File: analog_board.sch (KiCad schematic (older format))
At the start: 1 part

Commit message: Current measurement channels and connectors added
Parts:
- removed R?: R, symbol Device:R
- added C? (x2): 1n, symbol Device:C
- added C? (x6): 0.1u, symbol Device:C
- added C? (x6): 10u, symbol Device:C
- added D? (x2): LM385Z-1.2, Package_TO_SOT_THT:TO-92_Inline, symbol Reference_Voltage:LM385Z-1.2
- added J301, J302, J303, J304: SAMTEC-TSW-105-07-X-D, SAMTEC-TSW-105-07-X-D, symbol SAMTEC-TSW-105-07-X-D:SAMTEC-TSW-105-07-X-D
- added J? (x2): Conn_01x03_Male, symbol Connector:Conn_01x03_Male
- added R? (x2): 10M, symbol Device:R
- added R? (x6): 10R, symbol Device:R
- added R? (x2): 470R, symbol Device:R
- added R? (x4): 1k, symbol Device:R
- added R? (x2): 1k5, symbol Device:R
- added U? (x2): AD620, symbol Amplifier_Instrumentation:AD620
- added U? (x5): LM324, symbol Amplifier_Operational:LM324
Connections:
- net +15V: now also C?.1, C?.1, C?.1, C?.1, C?.1, C?.1, J301.7, J?.1 (Pin_1), J?.1 (Pin_1), U?.4 (V+), U?.7 (Vs+), U?.7 (Vs+)
- net GND: now also C?.1, C?.1, C?.2, C?.2, C?.2, C?.2, C?.2, C?.2, C?.2, C?.2, C?.2, C?.2, C?.2, C?.2, D?.2 (K), D?.2 (K), R?.1, R?.1, R?.1, R?.1, R?.1, R?.1, R?.2, R?.2, U?.2 (-), U?.2 (-), U?.2 (-), U?.2 (-)
- new net: R?.1, U?.1 (Rg) (x2)
- new net: C?.2, R?.1, U?.3 (+) (x2)
- new net: U?.1, U?.5 (Ref) (x2)
- new net: U?.5 (+), U?.6 (x2)
- new net: R?.2, U?.8 (Rg) (x2)
- new net: D?.3 (A), R?.1 (x2)
- new net: R?.1, R?.2 (x2)
- new net: R?.1, R?.2, U?.3 (+) (x2)
- new net +5V: J301.1
- new net -15V: C?.1, C?.1, C?.1, C?.1, C?.1, C?.1, J301.9, J?.3 (Pin_3), J?.3 (Pin_3), U?.11 (V-), U?.4 (Vs-), U?.4 (Vs-)
- new net 3V3_REF: J301.5
- new net 5V_REF: J301.3
- new net Current_ch1_out: U?.6 (-), U?.7
- new net Current_ch2_out: U?.6 (-), U?.7
- new net Current_ch_1_out: J303.1
- new net Current_ch_2_out: J303.3
- new net Current_sensor_1: J302.1, J?.2 (Pin_2), R?.2, R?.2, R?.2, R?.2
- new net Current_sensor_2: J302.3, J?.2 (Pin_2), R?.2, R?.2, R?.2, R?.2
- new net DIG1: J304.1
- new net DIG2: J304.3
- new net DIG3: J304.5
- new net DIG4: J304.7
- new net DIG5: J304.9
- new net Torque_pedal_ADC: J303.5
- new net Torque_pedal_in: J302.5

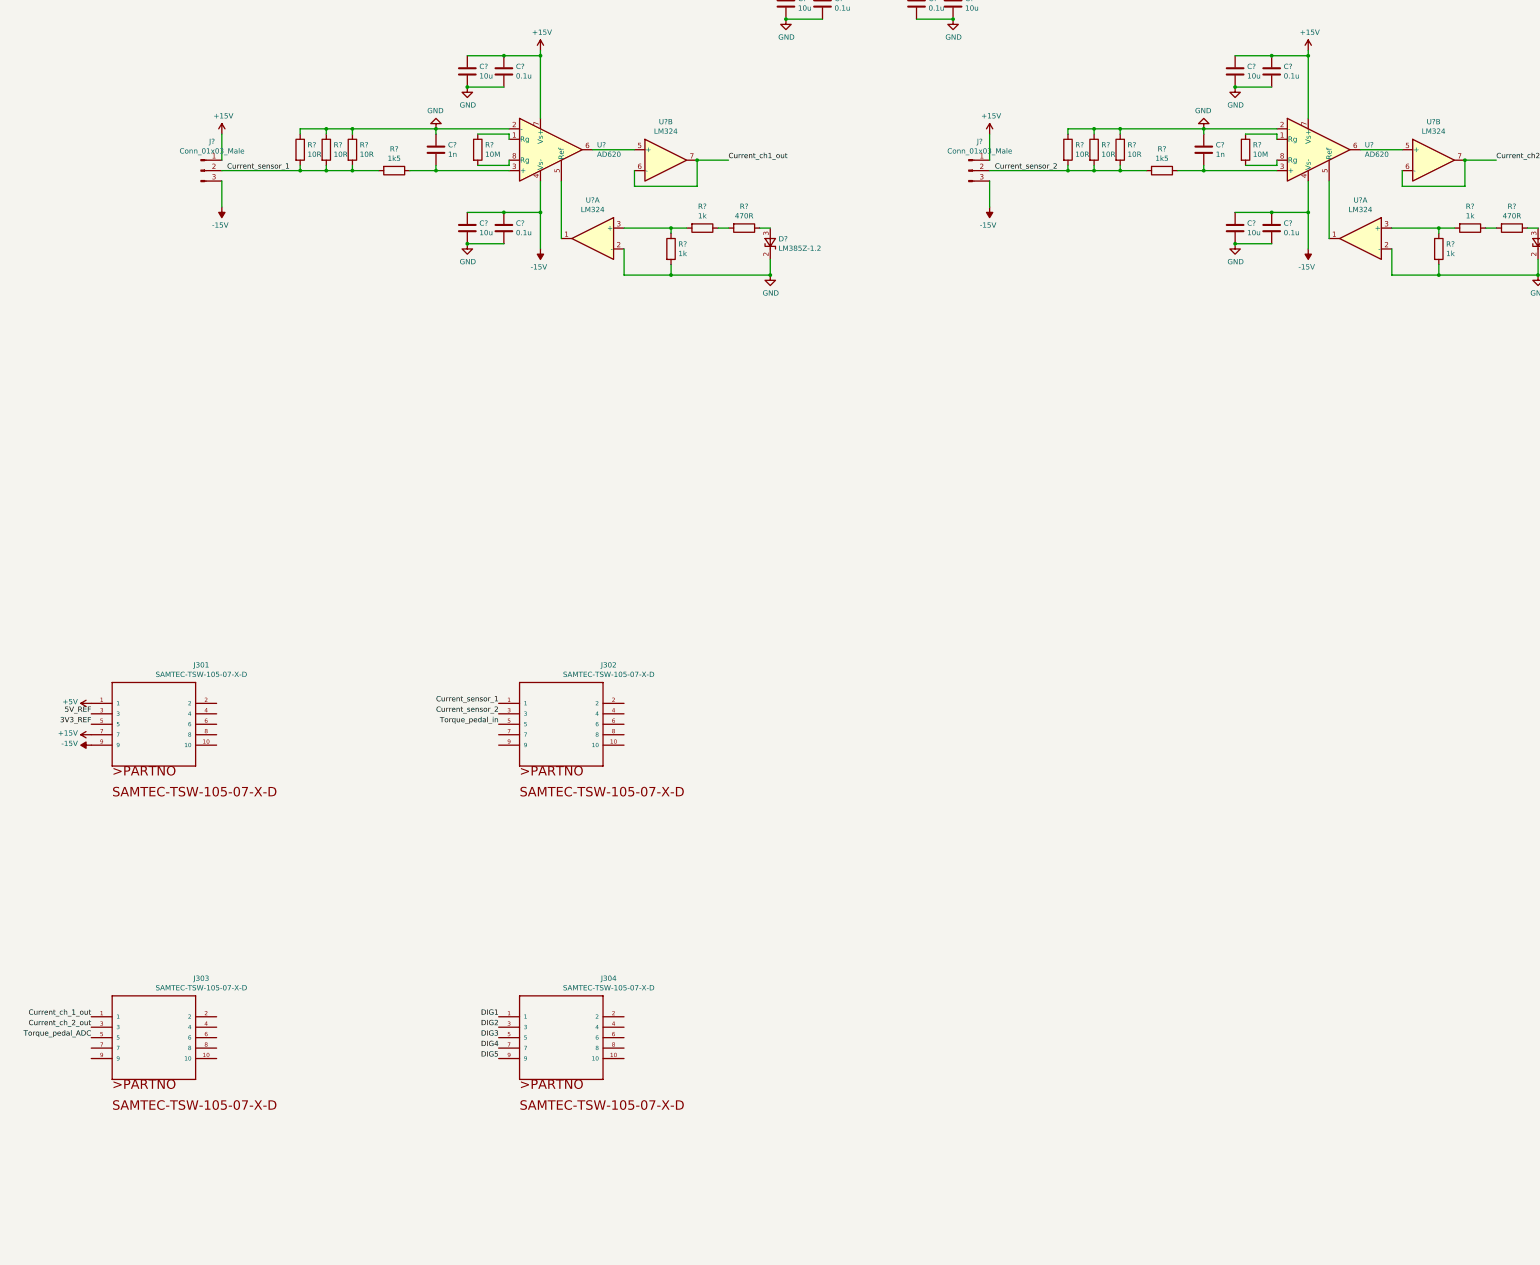
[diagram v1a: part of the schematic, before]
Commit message: Current measurement input filters, torque pedal reading
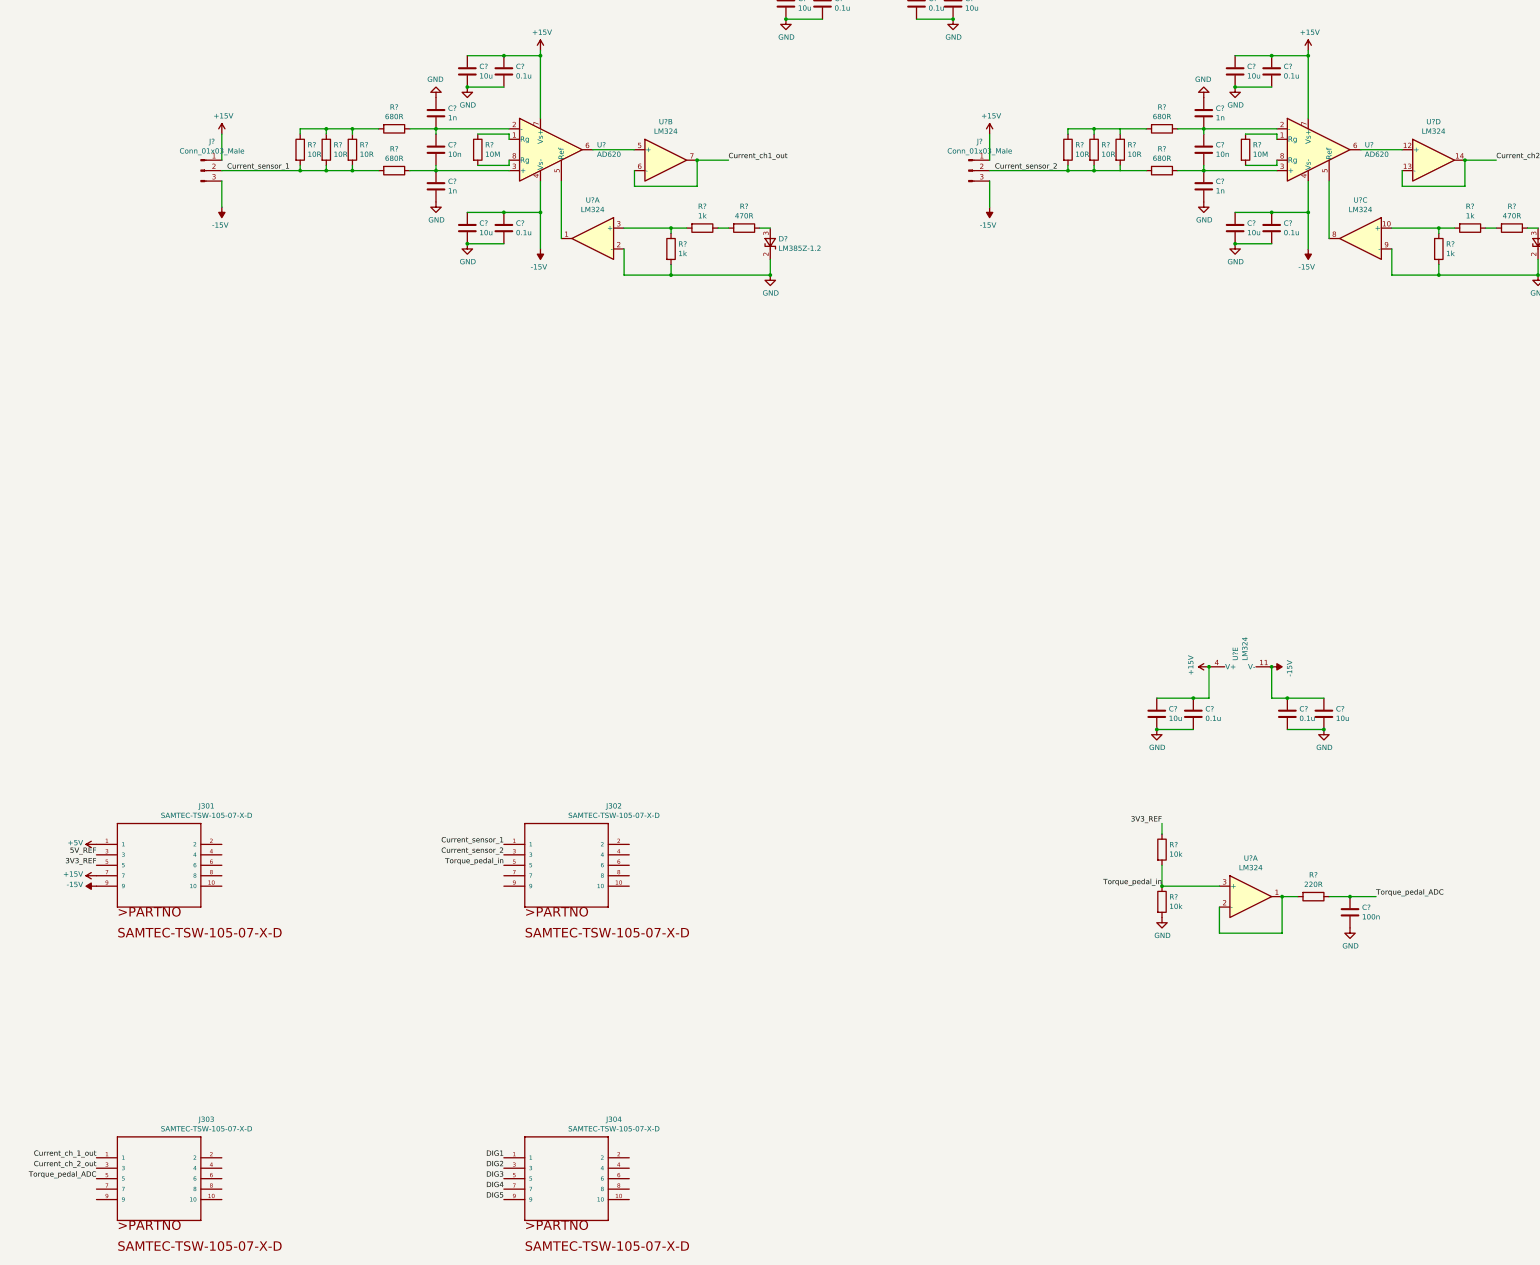
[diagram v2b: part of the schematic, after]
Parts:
- removed C?: 1n, symbol Device:C
- removed R?: 1k5, symbol Device:R
- removed U? (x2): LM324, symbol Amplifier_Operational:LM324
- added C? (x4): 1n, symbol Device:C
- added C?: 10n, symbol Device:C
- added C? (x2): 0.1u, symbol Device:C
- added C? (x2): 10u, symbol Device:C
- added C?: 100n, symbol Device:C
- added R? (x3): 680R, symbol Device:R
- added R?: 220R, symbol Device:R
- added R? (x2): 10k, symbol Device:R
- added U? (x4): LM324, symbol Amplifier_Operational:LM324
- C?: value 1n -> 10n
- R?: value 1k5 -> 680R
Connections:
- net +15V: now also C?.1, C?.1, U?.4 (V+)
- net -15V: now also C?.1, C?.1, U?.11 (V-)
- net 3V3_REF: now also R?.1
- net Current_ch2_out: now also U?.13 (-), U?.14
- net Current_sensor_2: now also R?.2
- net GND: now also C?.1, C?.1, C?.2, C?.2, C?.2, C?.2, C?.2, C?.2, C?.2, R?.2, U?.9 (-); no longer C?.1, R?.1, R?.1, R?.1, R?.1, R?.1, R?.1, U?.2 (-), U?.2 (-)
- net Torque_pedal_ADC: now also C?.1, R?.1
- net Torque_pedal_in: now also R?.1, R?.2, U?.3 (+)
- net at C?.2, R?.1, U?.3 (+): now also C?.1
- net at U?.3 (+): now also C?.1, C?.2, R?.1
- net at U?.5 (Ref): now also U?.8
- net at U?.6: now also U?.12 (+)
- net at R?.1, R?.2: now also U?.10 (+)
- new net: C?.1, C?.2, R?.1, U?.2 (-) (x2)
- new net: R?.1, R?.1, R?.1, R?.2 (x2)
- new net: R?.2, U?.1, U?.2 (-)
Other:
- moved on the sheet: J301, J302, J303, J304

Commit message: Added output filters and fixed reference opamp
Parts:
- removed C? (x2): 0.1u, symbol Device:C
- removed C? (x2): 10u, symbol Device:C
- removed D? (x2): LM385Z-1.2, Package_TO_SOT_THT:TO-92_Inline, symbol Reference_Voltage:LM385Z-1.2
- removed R? (x2): 10M, symbol Device:R
- removed R? (x2): 470R, symbol Device:R
- removed R? (x4): 1k, symbol Device:R
- removed U?: LM324, symbol Amplifier_Operational:LM324
- added C? (x4): 100n, symbol Device:C
- added C? (x2): 0.1u, symbol Device:C
- added C? (x2): 10u, symbol Device:C
- added D? (x2): LM385Z-1.2, Package_TO_SOT_THT:TO-92_Inline, symbol Reference_Voltage:LM385Z-1.2
- added R? (x2): 3k3, symbol Device:R
- added R? (x4): 220R, symbol Device:R
- added R? (x4): 1k, symbol Device:R
- added R? (x2): 470R, symbol Device:R
- added U? (x3): LM324, symbol Amplifier_Operational:LM324
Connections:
- net +15V: now also C?.1, C?.1, U?.4 (V+)
- net -15V: now also C?.1, C?.1, U?.11 (V-)
- net 3V3_REF: now also R?.1, R?.1
- net Current_ch1_out: now also C?.1, R?.1; no longer U?.6 (-), U?.7
- net Current_ch2_out: now also C?.1, R?.1; no longer U?.13 (-), U?.14
- net GND: now also R?.1, R?.1, R?.1, R?.1, R?.1, R?.1, R?.2, R?.2, C?.2, C?.2, C?.2, C?.2, C?.2, C?.2, C?.2, C?.2, D?.3 (A), D?.3 (A), R?.2, R?.2; no longer U?.2 (-), U?.9 (-)
- net at U?.1, U?.5 (Ref): now also U?.2 (-)
- net at U?.6: now also R?.2; no longer U?.5 (+)
- net at U?.3 (+): now also R?.1, R?.1
- net at U?.5 (Ref), U?.8: now also U?.9 (-)
- net at U?.6: now also R?.2; no longer U?.12 (+)
- net at U?.10 (+): now also R?.1, R?.1
- new net: C?.1, R?.1, U?.5 (+)
- new net: R?.2, U?.6 (-), U?.7
- new net: D?.2 (K), R?.2, U?.3 (+) (x2)
- new net: C?.1, R?.1, U?.12 (+)
- new net: R?.2, U?.13 (-), U?.14
- new net: R?.2, U?.1, U?.2 (-) (x2)
- new net: R?.1, R?.2 (x2)
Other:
- moved on the sheet: C?, J?, R?, U?, U?A, U?B, U?C, U?D, U?E

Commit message: Fixed opamp parts to the corresponding package
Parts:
- gave numbers to parts that had none: 2
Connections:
- net Torque_pedal_in: now also U1.12 (+); no longer U1.3 (+)
- net at R?.1, R?.1: now also U1.5 (+); no longer U1.3 (+)
- net at C?.1, R?.1: now also U1.3 (+); no longer U1.5 (+)
- net at D?.2 (K), R?.2: now also U1.10 (+); no longer U1.3 (+)
- net at R?.1, R?.1: now also U2.5 (+); no longer U2.10 (+)
- net at C?.1, R?.1: now also U2.3 (+); no longer U2.12 (+)
- net at D?.2 (K), R?.2: now also U2.10 (+); no longer U2.3 (+)
- new net: U1.6 (-), U1.7, U?.5 (Ref)
- new net: R?.2, U1.1, U1.2 (-)
- new net: U2.6 (-), U2.7, U?.5 (Ref)
- new net: R?.2, U1.13 (-), U1.14
- new net: R?.2, U2.1, U2.2 (-)
- new net: R?.2, U1.8, U1.9 (-)
- new net: R?.2, U2.8, U2.9 (-)
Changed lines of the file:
@@
 Current_sensor_1
 $Comp
-L Amplifier_Operational:LM324 U?
-U 1 1 5C6FEAFE
+L Amplifier_Operational:LM324 U1
+U 2 1 5C6FEAFE
 P 4950 6000
-F 0 "U?" H 4950 6367 50  0000 C CNN
+F 0 "U1" H 4950 6367 50  0000 C CNN
 F 1 "LM324" H 4950 6276 50  0000 C CNN
 F 2 "" H 4900 6100 50  0001 C CNN
 F 3 "http://www.ti.com/lit/ds/symlink/lm2902-n.pdf" H 5000 6200 50  0001 C CNN
-	1    4950 6000
+	2    4950 6000
 	-1   0    0    -1
 $EndComp
@@
 	5250 6100 5250 6350
 $Comp
-L Amplifier_Operational:LM324 U?
-U 2 1 5C7012E7
+L Amplifier_Operational:LM324 U1
+U 1 1 5C7012E7
 P 6350 4700
-F 0 "U?" H 6350 5067 50  0000 C CNN
+F 0 "U1" H 6350 5067 50  0000 C CNN
 F 1 "LM324" H 6350 4976 50  0000 C CNN
 F 2 "" H 6300 4800 50  0001 C CNN
 F 3 "http://www.ti.com/lit/ds/symlink/lm2902-n.pdf" H 6400 4900 50  0001 C CNN
-	2    6350 4700
+	1    6350 4700
 	1    0    0    -1
 $EndComp
@@
 	12600 4900 12600 5150
 $Comp
-L Amplifier_Operational:LM324 U?
+L Amplifier_Operational:LM324 U1
 U 5 1 5C746485
 P 4450 950
-F 0 "U?" H 4408 996 50  0000 L CNN
+F 0 "U1" H 4408 996 50  0000 L CNN
 F 1 "LM324" H 4408 905 50  0000 L CNN
 F 2 "" H 4400 1050 50  0001 C CNN
@@
 $EndComp
 $Comp
-L Amplifier_Operational:LM324 U?
-U 1 1 5C73D7CC
+L Amplifier_Operational:LM324 U1
+U 4 1 5C73D7CC
 P 14650 12300
-F 0 "U?" H 14650 12667 50  0000 C CNN
+F 0 "U1" H 14650 12667 50  0000 C CNN
 F 1 "LM324" H 14650 12576 50  0000 C CNN
 F 2 "" H 14600 12400 50  0001 C CNN
 F 3 "http://www.ti.com/lit/ds/symlink/lm2902-n.pdf" H 14700 12500 50  0001 C CNN
-	1    14650 12300
+	4    14650 12300
 	1    0    0    -1
 $EndComp
@@
 	13800 11700 13800 11600
 $Comp
-L Amplifier_Operational:LM324 U?
-U 3 1 5C78DB94
+L Amplifier_Operational:LM324 U2
+U 2 1 5C78DB94
 P 16150 6000
-F 0 "U?" H 16150 6367 50  0000 C CNN
+F 0 "U2" H 16150 6367 50  0000 C CNN
 F 1 "LM324" H 16150 6276 50  0000 C CNN
 F 2 "" H 16100 6100 50  0001 C CNN
 F 3 "http://www.ti.com/lit/ds/symlink/lm2902-n.pdf" H 16200 6200 50  0001 C CNN
-	3    16150 6000
+	2    16150 6000
 	-1   0    0    -1
 $EndComp
 $Comp
-L Amplifier_Operational:LM324 U?
-U 4 1 5C7949F2
+L Amplifier_Operational:LM324 U2
+U 1 1 5C7949F2
 P 17550 4700
-F 0 "U?" H 17550 5067 50  0000 C CNN
+F 0 "U2" H 17550 5067 50  0000 C CNN
 F 1 "LM324" H 17550 4976 50  0000 C CNN
 F 2 "" H 17500 4800 50  0001 C CNN
 F 3 "http://www.ti.com/lit/ds/symlink/lm2902-n.pdf" H 17600 4900 50  0001 C CNN
-	4    17550 4700
+	1    17550 4700
 	1    0    0    -1
 $EndComp
@@
 Connection ~ 7250 5800
 $Comp
-L Amplifier_Operational:LM324 U?
-U 1 1 5C7A4403
+L Amplifier_Operational:LM324 U1
+U 3 1 5C7A4403
 P 6600 5900
-F 0 "U?" H 6600 6267 50  0000 C CNN
+F 0 "U1" H 6600 6267 50  0000 C CNN
 F 1 "LM324" H 6600 6176 50  0000 C CNN
 F 2 "" H 6550 6000 50  0001 C CNN
 F 3 "http://www.ti.com/lit/ds/symlink/lm2902-n.pdf" H 6650 6100 50  0001 C CNN
-	1    6600 5900
+	3    6600 5900
 	-1   0    0    -1
 $EndComp
@@
 Connection ~ 17850 4700
 $Comp
-L Amplifier_Operational:LM324 U?
+L Amplifier_Operational:LM324 U2
 U 5 1 5C80F4D6
 P 15700 950
-F 0 "U?" H 15658 996 50  0000 L CNN
+F 0 "U2" H 15658 996 50  0000 L CNN
 F 1 "LM324" H 15658 905 50  0000 L CNN
 F 2 "" H 15650 1050 50  0001 C CNN
@@
 Connection ~ 18450 5800
 $Comp
-L Amplifier_Operational:LM324 U?
-U 1 1 5C873DA1
+L Amplifier_Operational:LM324 U2
+U 3 1 5C873DA1
 P 17800 5900
-F 0 "U?" H 17800 6267 50  0000 C CNN
+F 0 "U2" H 17800 6267 50  0000 C CNN
 F 1 "LM324" H 17800 6176 50  0000 C CNN
 F 2 "" H 17750 6000 50  0001 C CNN
 F 3 "http://www.ti.com/lit/ds/symlink/lm2902-n.pdf" H 17850 6100 50  0001 C CNN
-	1    17800 5900
+	3    17800 5900
 	-1   0    0    -1
 $EndComp

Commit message: Some footprints added, removed unnecessary REF opamps
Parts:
- removed J? (x2): Conn_01x03_Male, symbol Connector:Conn_01x03_Male
- removed unit 3 of U1
- removed unit 3 of U2
- C1, C10, C11, C12, C13, C14, C15, C16, C17, C18, C19, C2, C20, C21, C22, C23, C24, C25, C26, C27, C3, C4, C5, C6, C7, C8, C9: renamed from C?; footprint (none) -> Capacitor_SMD:C_0805_2012Metric_Pad1.15x1.40mm_HandSolder
- R1, R10, R11, R12, R13, R14, R15, R16, R17, R18, R19, R2, R20, R21, R22, R23, R24, R25, R3, R4, R5, R6, R7, R8, R9: renamed from R?; footprint (none) -> Resistor_SMD:R_0805_2012Metric_Pad1.15x1.40mm_HandSolder
- gave numbers to parts that had none: 4
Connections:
- net at D1.2 (K), R11.2: now also R9.2
- net at D2.2 (K), R25.2: now also R23.2
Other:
- moved on the sheet: D1, D2, R11, R25

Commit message: Mapped AIB-to-MB connector pins, assigned footprints
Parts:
- J301, J302, J304: footprint SAMTEC-TSW-105-07-X-D -> Connector_PinSocket_2.54mm:PinSocket_2x05_P2.54mm_Vertical
- J305: renamed from J303; footprint SAMTEC-TSW-105-07-X-D -> Connector_PinSocket_2.54mm:PinSocket_2x05_P2.54mm_Vertical
- U1, U2: footprint (none) -> Package_DIP:DIP-14_W7.62mm
- U1: renamed from U2; footprint (none) -> Package_DIP:DIP-14_W7.62mm
- U2: renamed from U1; footprint (none) -> Package_DIP:DIP-14_W7.62mm
- U3, U4: footprint (none) -> Package_DIP:DIP-8_W7.62mm
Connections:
- net +15V: now also J301.8; no longer J301.7
- net +5V: now also J301.2; no longer J301.1
- net -15V: now also J301.10; no longer J301.9
- net 3V3_REF: now also J301.6; no longer J301.5
- net 5V_REF: now also J301.4; no longer J301.3
- net Current_ch_1_out: now also J304.9; no longer J305.1
- net Current_ch_2_out: now also J304.7; no longer J305.3
- net Current_sensor_1: now also J302.2; no longer J302.1
- net Current_sensor_2: now also J302.4; no longer J302.3
- net DIG1: now also J305.9; no longer J304.1
- net DIG2: now also J305.7; no longer J304.3
- net DIG3: now also J305.5; no longer J304.5
- net DIG4: now also J305.3; no longer J304.7
- net DIG5: now also J305.1; no longer J304.9
- net GND: now also J301.1, J301.3, J301.5, J301.7, J301.9, J302.1, J302.3, J302.5, J302.7, J302.9, J304.10, J304.2, J304.4, J304.6, J304.8, J305.10, J305.2, J305.4, J305.6, J305.8
- net Torque_pedal_ADC: now also J304.5; no longer J305.5
- net Torque_pedal_in: now also J302.6, U2.3 (+); no longer J302.5, U2.12 (+)
- net at R21.1, R22.1: now also U1.12 (+); no longer U1.5 (+)
- net at C26.1, R20.1: now also U1.10 (+); no longer U1.3 (+)
- new net: U1.13 (-), U1.14, U4.5 (Ref)
- new net: R19.2, U2.1, U2.2 (-)
- new net: R24.2, U1.8, U1.9 (-)
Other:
- moved on the sheet: C17, C20, C24, C25, U2E

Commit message: Begun layout
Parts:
- removed C13, C27: 100n, Capacitor_SMD:C_0805_2012Metric_Pad1.15x1.40mm_HandSolder, symbol Device:C
- removed C17, C25: 10u, Capacitor_SMD:C_0805_2012Metric_Pad1.15x1.40mm_HandSolder, symbol Device:C
- removed C20, C24: 0.1u, Capacitor_SMD:C_0805_2012Metric_Pad1.15x1.40mm_HandSolder, symbol Device:C
- removed R10, R24: 220R, Resistor_SMD:R_0805_2012Metric_Pad1.15x1.40mm_HandSolder, symbol Device:R
- removed unit 1 of U1
- removed unit 3 of U1
- removed unit 5 of U2
- renumbered U2 to U1
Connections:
- net Current_ch_1_out is gone; now on net Current_ch1_out: J304.9
- net Current_ch_2_out is gone; now on net Current_ch2_out: J304.7
- net Current_ch1_out: now also C12.1, R6.1
- net Current_ch2_out: now also C26.1, R20.1
- net Torque_pedal_in: now also U1.10 (+); no longer U1.3 (+)
- net at R7.1, R8.1: now also U1.3 (+); no longer U1.5 (+)
- net at R21.1, R22.1: now also U1.5 (+); no longer U1.12 (+)
- new net: U1.1, U1.2 (-), U3.5 (Ref)
- new net: U1.6 (-), U1.7, U4.5 (Ref)
- new net: R19.2, U1.8, U1.9 (-)
- no-connect marks 0 -> 14
